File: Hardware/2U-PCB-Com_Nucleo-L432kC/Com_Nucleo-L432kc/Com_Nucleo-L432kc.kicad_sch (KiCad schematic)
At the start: 29 parts, among them IC1 PCI_EXPRESS_CARD, J1 Bus Standard, J2 Calculatrice_UART_groove, J3 RAK5146_UART_groove(GPS), J4 RAK5146_SPI_groove(MCU), J5 RAK5146_I2C_groove(GPS), Q2 BC807

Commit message: L9616 in the library. This version we still have the GPS signal. From now on I'll let the main withou the GPS signals, because the sensor cards have already one GPS.
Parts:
- added C10: 100n, Capacitor_SMD:C_0402_1005Metric, symbol Device:C
- added C9: 10u, Capacitor_SMD:C_0603_1608Metric, symbol Device:C
- added CR1: L9616, footprints:SO-8_STM, symbol 2023-06-06_07-55-18:L9616
- added J6, J7: Conn_01x15, Connector_PinSocket_2.54mm:PinSocket_1x15_P2.54mm_Vertical, symbol Connector_Generic:Conn_01x15
- added JP4: Jumper_RESET_L432KC_Open, Button_Switch_SMD:SW_Push_1P1T_NO_CK_KMR2, symbol Jumper:Jumper_2_Open
- added RV1: R_Potentiometer_Trim, Potentiometer_SMD:Potentiometer_ACP_CA6-VSMD_Vertical, symbol Device:R_Potentiometer_Trim
- renumbered C5 to C4, C7 to C5, C8 to C6, C4 to C7, C6 to C8
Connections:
- net +3V3: now also C10.1, C9.1, CR1.3 (VS), RV1.1
- net CAN1_RX: now also CR1.4 (RX0), J7.13 (Pin_13)
- net CAN1_TX: now also CR1.1 (TX0), J7.5 (Pin_5)
- net GND: now also C10.2, C9.2, CR1.2 (GND), J6.2 (Pin_2), J7.4 (Pin_4), JP4.2 (B), RV1.3
- net HOST_CSN: now also J7.15 (Pin_15)
- net HOST_MISO: now also J6.7 (Pin_7)
- net HOST_MOSI: now also J6.6 (Pin_6)
- net HOST_SCK: now also J6.11 (Pin_11)
- net L432KC_RESET: now also J6.3 (Pin_3), J7.3 (Pin_3), JP4.1 (A)
- net MCU_NRESET: now also J7.14 (Pin_14)
- net PWM_MAG-Y: now also J7.6 (Pin_6); no longer L432KC1.21 (A2)
- net PWM_ROUE/MAG-X: now also J7.12 (Pin_12)
- net RESET_SIGNAL: now also J6.8 (Pin_8)
- net RX_CALC: now also J7.8 (Pin_8)
- net SCL: now also J7.1 (Pin_1)
- net SDA: now also J7.2 (Pin_2)
- net SENS_MAG-Y: now also J6.15 (Pin_15)
- net SENS_ROUE/MAG-X: now also J6.12 (Pin_12)
- net SX1303_GPIO_8: now also J7.9 (Pin_9)
- net TX_CALC: now also J7.7 (Pin_7)
- net Vin: now also J6.1 (Pin_1)
- net at L432KC1.17 (+3V3): now also J6.14 (Pin_14)
- net at L432KC1.18 (AREF): now also J6.13 (Pin_13)
- net C_LOW: now reaches L432KC1.22 (A3)
- net C_LOW: now also CR1.6 (C_L), J6.9 (Pin_9)
- net C_HIGH: now reaches L432KC1.26 (A7)
- net C_HIGH: now also CR1.7 (C_H), J6.5 (Pin_5)
- net at L432KC1.27 (+5V): now also J6.4 (Pin_4)
- new net: J6.10 (Pin_10), L432KC1.21 (A2)
- new net: CR1.8 (ASC), RV1.2
- no-connect marks 36 -> 39
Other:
- moved on the sheet: C7, C8, IC1, J1, J2, J3, J4, J5, JP1, JP2, JP3, L432KC1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

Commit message: This version also has no GPS I2C labe, nor USB, that has no prevision for use in this version at least.
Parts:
- removed J3: RAK5146_UART_groove(GPS), Connector_PinSocket_2.54mm:PinSocket_1x05_P2.54mm_Vertical, symbol Connector_Generic:Conn_01x05
- removed J5: RAK5146_I2C_groove(GPS), Connector_PinSocket_2.54mm:PinSocket_1x05_P2.54mm_Vertical, symbol Connector_Generic:Conn_01x05
- removed R2, R6, R7: 100, Resistor_SMD:R_0402_1005Metric, symbol Device:R
- removed R3: 0, Resistor_SMD:R_0402_1005Metric, symbol Device:R
- R3: renamed from R8; value 100 -> 100K
- renumbered R4 to R2, R5 to R4, R9 to R7, R10 to R8
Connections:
- net GND: no longer JP3.1 (A), Q2.3 (C), R8.1
- net SX1303_RESET: now reaches IC1.22 (~{PERST}), R3.1
- net SX1303_RESET: now also JP3.1 (A), Q2.3 (C), R8.1
- net STANDBY_GPS: no longer names the net of IC1.25 (PERp0)
- net UART_RX_GPS: no longer names the net of IC1.33 (PETp0)
- net UART_TX_GPS: no longer names the net of IC1.31 (PETn0)
- net USB_DM: no longer names the net of IC1.36 (USB_D-)
- net USB_DP: no longer names the net of IC1.38 (USB_D+)
- no-connect marks 39 -> 49
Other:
- moved on the sheet: J4

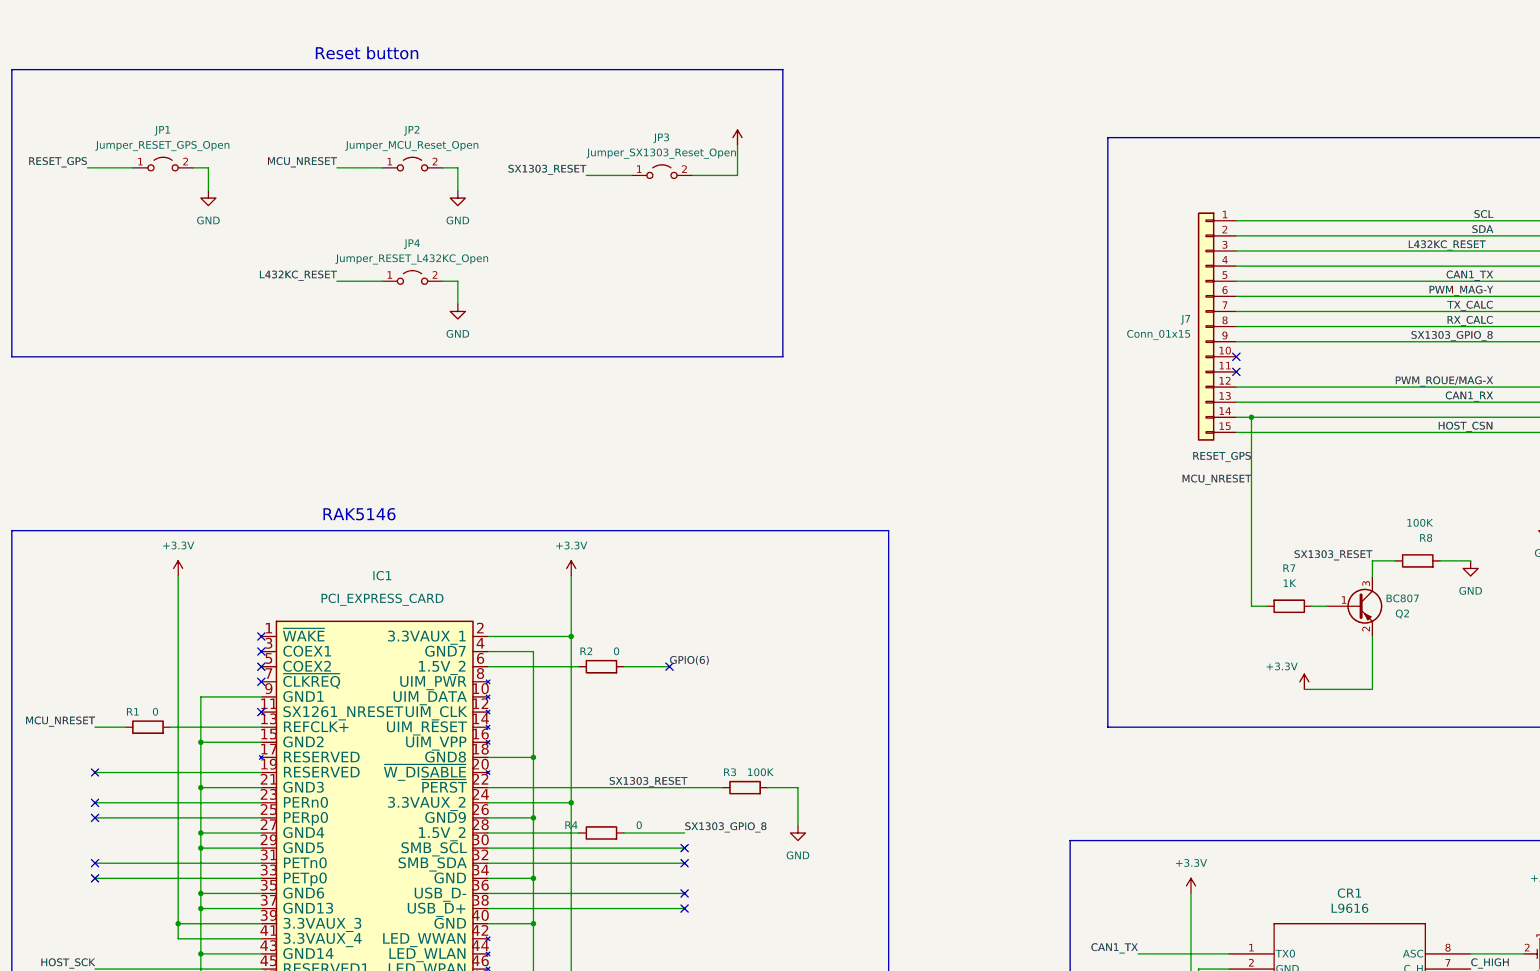
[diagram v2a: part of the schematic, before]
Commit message: Resistors number fixed. Schematic is ready to start routing. Some power routings are done.
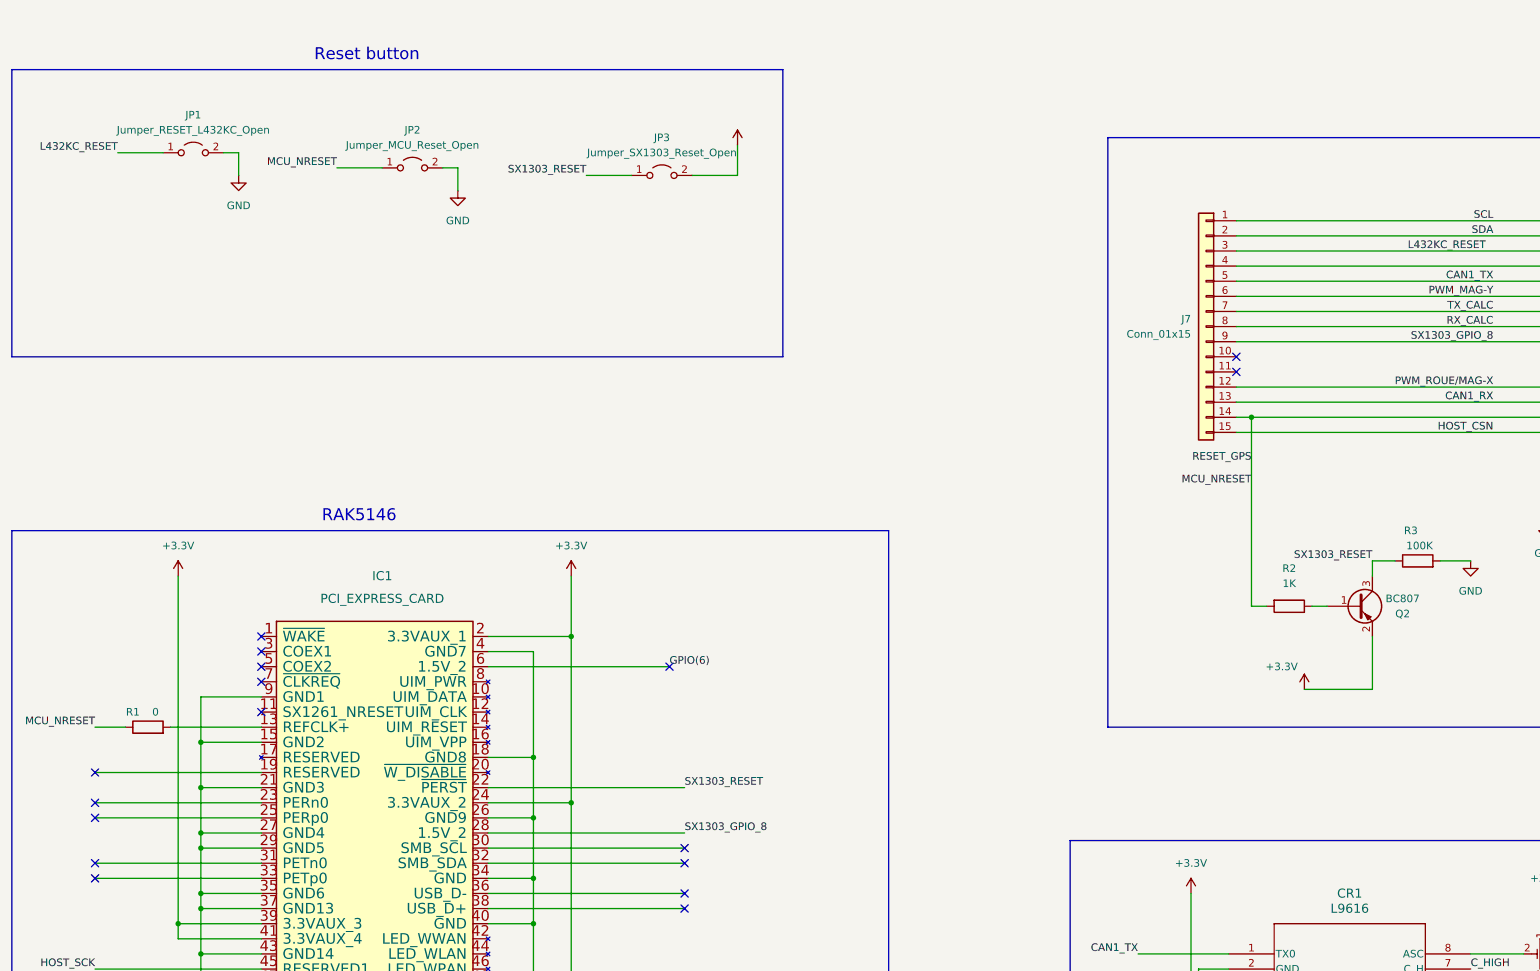
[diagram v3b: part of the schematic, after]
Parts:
- removed JP1: Jumper_RESET_GPS_Open, Button_Switch_SMD:SW_Push_1P1T_NO_CK_KMR2, symbol Jumper:Jumper_2_Open
- removed R2, R4: 0, Resistor_SMD:R_0402_1005Metric, symbol Device:R
- removed R3: 100K, Resistor_SMD:R_0402_1005Metric, symbol Device:R
- renumbered JP4 to JP1, R7 to R2, R8 to R3
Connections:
- net GPIO(6): now also IC1.6 (1.5V_2)
- net SX1303_GPIO_8: now also IC1.28 (1.5V_2)
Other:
- moved on the sheet: JP1

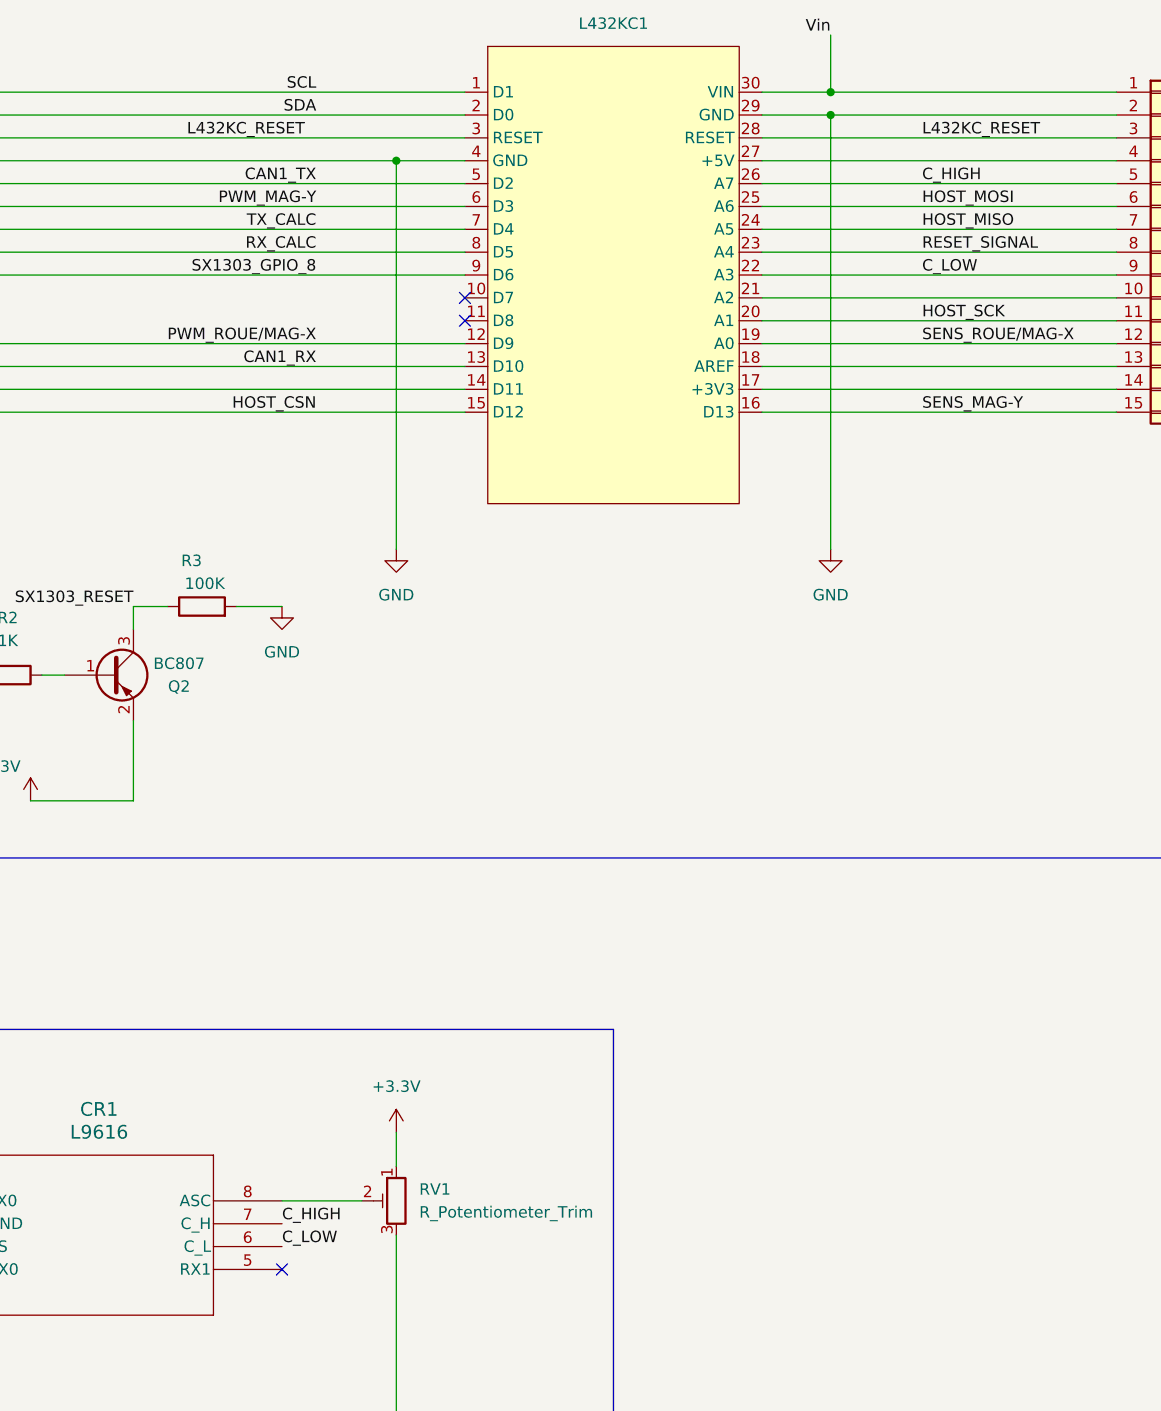
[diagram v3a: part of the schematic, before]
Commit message: Project name was wrong in in kicad files. Project renamed
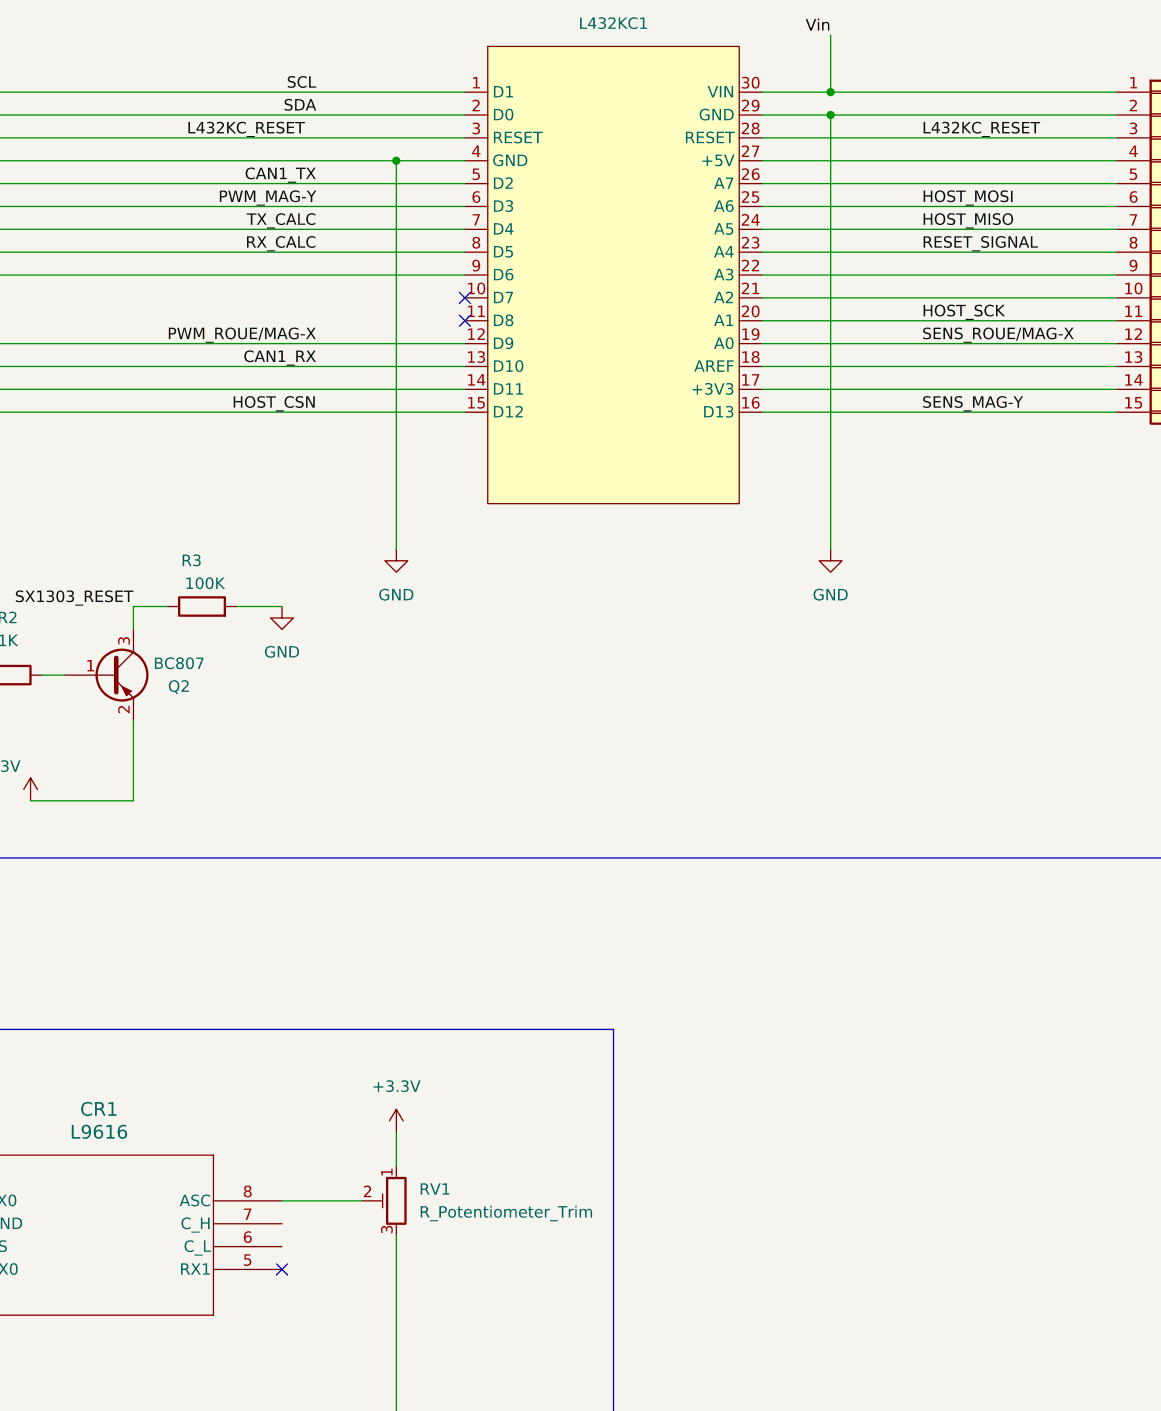
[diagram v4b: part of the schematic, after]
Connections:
- net SX1303_GPIO_8: no longer J7.9 (Pin_9), L432KC1.9 (D6)
- net C_HIGH: no longer names the net of J6.5 (Pin_5), L432KC1.26 (A7)
- net C_HIGH: no longer CR1.7 (C_H)
- net C_LOW: no longer names the net of J6.9 (Pin_9), L432KC1.22 (A3)
- net C_LOW: no longer CR1.6 (C_L)
- new net: J7.9 (Pin_9), L432KC1.9 (D6)
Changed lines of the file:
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@@
-    (effects (font (size 1.27 1.27)) (justify left bottom))
-  )
-  (label "C_LOW" (at 334.01 151.13 0) (fields_autoplaced)
     (effects (font (size 1.27 1.27)) (justify left bottom))
   )
@@
     (effects (font (size 1.27 1.27)) (justify right bottom))
   )
-  (label "C_HIGH" (at 262.89 256.54 0) (fields_autoplaced)
-    (effects (font (size 1.27 1.27)) (justify left bottom))
-  )
-  (label "C_LOW" (at 262.89 259.08 0) (fields_autoplaced)
-    (effects (font (size 1.27 1.27)) (justify left bottom))
-  )
   (label "CAN1_TX" (at 266.7 140.97 180) (fields_autoplaced)
     (effects (font (size 1.27 1.27)) (justify right bottom))
-  )
-  (label "C_HIGH" (at 334.01 140.97 0) (fields_autoplaced)
-    (effects (font (size 1.27 1.27)) (justify left bottom))
   )
   (label "MCU_NRESET" (at 31.75 215.9 180) (fields_autoplaced)
@@
     (effects (font (size 1.27 1.27)) (justify left bottom))
   )
-  (label "SX1303_GPIO_8" (at 266.7 151.13 180) (fields_autoplaced)
-    (effects (font (size 1.27 1.27)) (justify right bottom))
-  )
   (label "CAN1_TX" (at 207.01 254 180) (fields_autoplaced)

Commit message: Some libraries were added for NAND gate. Also I2C in mikrobus changed. ROuting started respecting constraints.
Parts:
- removed J4: RAK5146_SPI_groove(MCU), Connector_PinSocket_2.54mm:PinSocket_1x06_P2.54mm_Vertical, symbol Connector_Generic:Conn_01x06
- removed Q2: BC807, Package_TO_SOT_SMD:SOT-23, symbol Transistor_BJT:BC807
- removed RV1: R_Potentiometer_Trim, Potentiometer_SMD:Potentiometer_ACP_CA6-VSMD_Vertical, symbol Device:R_Potentiometer_Trim
- added B1, B2: SN74AHC1G125DBVT, Package_SO:TSOP-5_1.65x3.05mm_P0.95mm, symbol SN74AHC1:SN74AHC1
- added C11: 10u, Capacitor_SMD:C_0603_1608Metric, symbol Device:C
- added C12: 100n, Capacitor_SMD:C_0402_1005Metric, symbol Device:C
- added J3, J8, J9: I2C_Groove, Connector:NS-Tech_Grove_1x04_P2mm_Vertical, symbol Connector_Generic:Conn_01x04
- added J4, J5: Conn_01x08, Conn_mikro:MIkrobus_Connector, symbol Connector_Generic:Conn_01x08
- added JP4: Jumper_RESET_GPS_Open, Button_Switch_SMD:SW_Push_1P1T_NO_CK_KMR2, symbol Jumper:Jumper_2_Open
- added JP5: Jumper_STANDBY_GPS_Open, Connector_PinHeader_1.27mm:PinHeader_1x02_P1.27mm_Vertical, symbol Jumper:Jumper_2_Open
- added JP6: speed_controller, Connector_PinHeader_1.27mm:PinHeader_1x02_P1.27mm_Vertical, symbol Jumper:Jumper_2_Open
- added R4, R5, R6, R7: 100, Resistor_SMD:R_0402_1005Metric, symbol Device:R
- added R8, R9: 0, Resistor_SMD:R_0402_1005Metric, symbol Device:R
- added U2: 74LVC2G02, SN74LVC2G02_SSOP:DCT8, symbol 74xGxx:74LVC2G02
- J2: value Calculatrice_UART_groove -> I2C_Groove
- R2: value 1K -> 100
- R3: value 100K -> 0
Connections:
- net +3V3: now also B1.5 (VCC), B2.5 (VCC), C11.1, C12.1, J3.3 (Pin_3), J4.7 (Pin_7), J8.3 (Pin_3), J9.3 (Pin_3), JP6.2 (B), U2.8 (VCC)
- net GND: now also B1.3 (GND), B2.3 (GND), C11.2, C12.2, J3.4 (Pin_4), J4.8 (Pin_8), J5.8 (Pin_8), J8.4 (Pin_4), J9.4 (Pin_4), JP4.2 (B), JP5.2 (B), U2.4 (GND); no longer R3.2
- net GPIO(6): now also J6.10 (Pin_10), L432KC1.21 (A2), R8.2; no longer IC1.6 (1.5V_2)
- net HOST_MISO: now also B1.2 (A), R5.1; no longer IC1.47 (RESERVED2), J6.7 (Pin_7), L432KC1.24 (A5)
- net HOST_SCK: now also J4.4 (Pin_4), R4.1; no longer IC1.45 (RESERVED1)
- net MCU_NRESET: now also R3.1, J4.2 (Pin_2), JP4.1 (A), U2.5, U2.6; no longer R2.2
- net RX_CALC: no longer J2.2 (Pin_2)
- net SCL: now also IC1.30 (SMB_SCL), J2.2 (Pin_2), J3.1 (Pin_1), J5.5 (Pin_5), J8.1 (Pin_1), J9.1 (Pin_1)
- net SDA: now also IC1.32 (SMB_SDA), J2.3 (Pin_3), J3.2 (Pin_2), J5.6 (Pin_6), J8.2 (Pin_2), J9.2 (Pin_2)
- net SX1303_RESET: now also U2.3; no longer R3.1
- net TX_CALC: no longer J2.3 (Pin_3)
- net CAN_RD: now reaches J1.22 (RD)
- net CAN_RD: now also CR1.6 (C_L)
- net CAN_TD: now reaches J1.24 (TD)
- net CAN_TD: now also CR1.7 (C_H)
- net at IC1.19 (RESERVED): now also R2.2
- net at IC1.23 (PERn0): now also R3.2
- net STANDBY_GPS: now reaches IC1.25 (PERp0)
- net STANDBY_GPS: now also JP5.1 (A)
- net INT_MKR: now reaches J6.5 (Pin_5), L432KC1.26 (A7)
- net INT_MKR: now also J5.2 (Pin_2)
- net AN: now reaches J6.9 (Pin_9), L432KC1.22 (A3)
- net AN: now also J4.1 (Pin_1)
- net at CR1.8 (ASC): now also JP6.1 (A)
- net PWM_MKR: now reaches J7.9 (Pin_9), L432KC1.9 (D6)
- net PWM_MKR: now also J5.1 (Pin_1)
- net HOST_CSN renamed CS_MCU
- net CS_MCU: now also B1.1 (OE), J4.3 (Pin_3), R7.1, U2.1, U2.2; no longer IC1.51 (RESERVED4)
- net HOST_MOSI renamed MCU_MOSI
- net MCU_MOSI: now also J4.6 (Pin_6), R6.1; no longer IC1.49 (RESERVED3)
- net SX1303_GPIO_8: no longer names the net of IC1.28 (1.5V_2)
- net SX1303_GPIO_8: now also R9.1
- new net: B2.1 (OE), U2.7
- new net: IC1.51 (RESERVED4), R7.2
- new net: IC1.45 (RESERVED1), R4.2
- new net: IC1.47 (RESERVED2), R5.2
- new net: IC1.49 (RESERVED3), R6.2
- new net: IC1.6 (1.5V_2), R8.1
- new net MISO: B1.4 (Y), B2.4 (Y), J6.7 (Pin_7), L432KC1.24 (A5)
- new net MKB_MISO: B2.2 (A), J4.5 (Pin_5)
- no-connect marks 49 -> 46
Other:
- note added: "CAN Buffer"
- note added: "Decoupling and bolt capacitors for Nucleo"
- note added: "MCU"
- note added: "Mikrobus"
- note removed: "Decoupling and bolt capacitors for ESP32"
- moved on the sheet: C10, C9, IC1, R1
